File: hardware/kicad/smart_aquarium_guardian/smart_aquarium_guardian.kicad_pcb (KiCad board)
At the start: 2 copper layers, 110 x 90 mm, 30 parts, among them J1 Display_2.8_TFT_240xRGBx320, J2 Tiny_RTC_I2C_Module, J3 SensorsInput, J4 TdsMeter, J5 PowerSupply, M1 MountingHole_3.5mm, M2 MountingHole_3.5mm, M3 MountingHole_3.5mm, M4 MountingHole_3.5mm

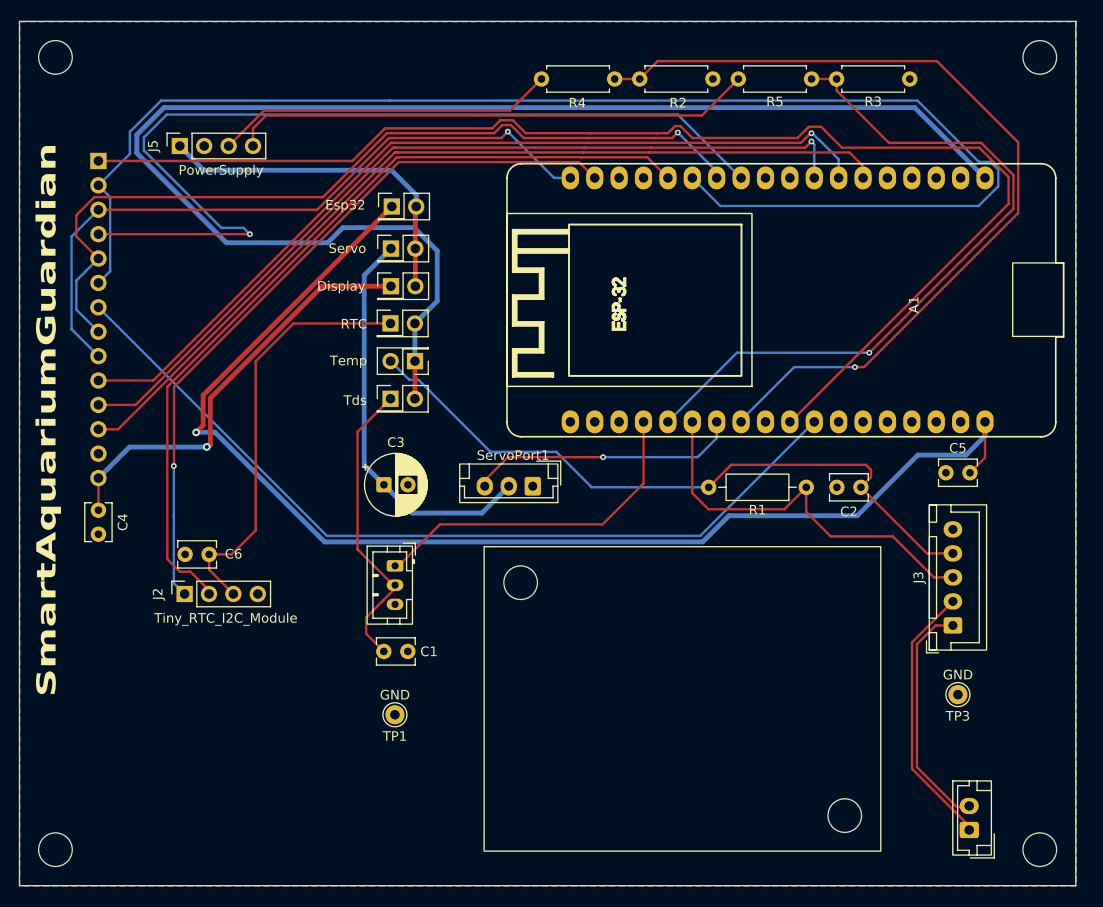
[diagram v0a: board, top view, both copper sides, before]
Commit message: Changes made after recommendations before printing it
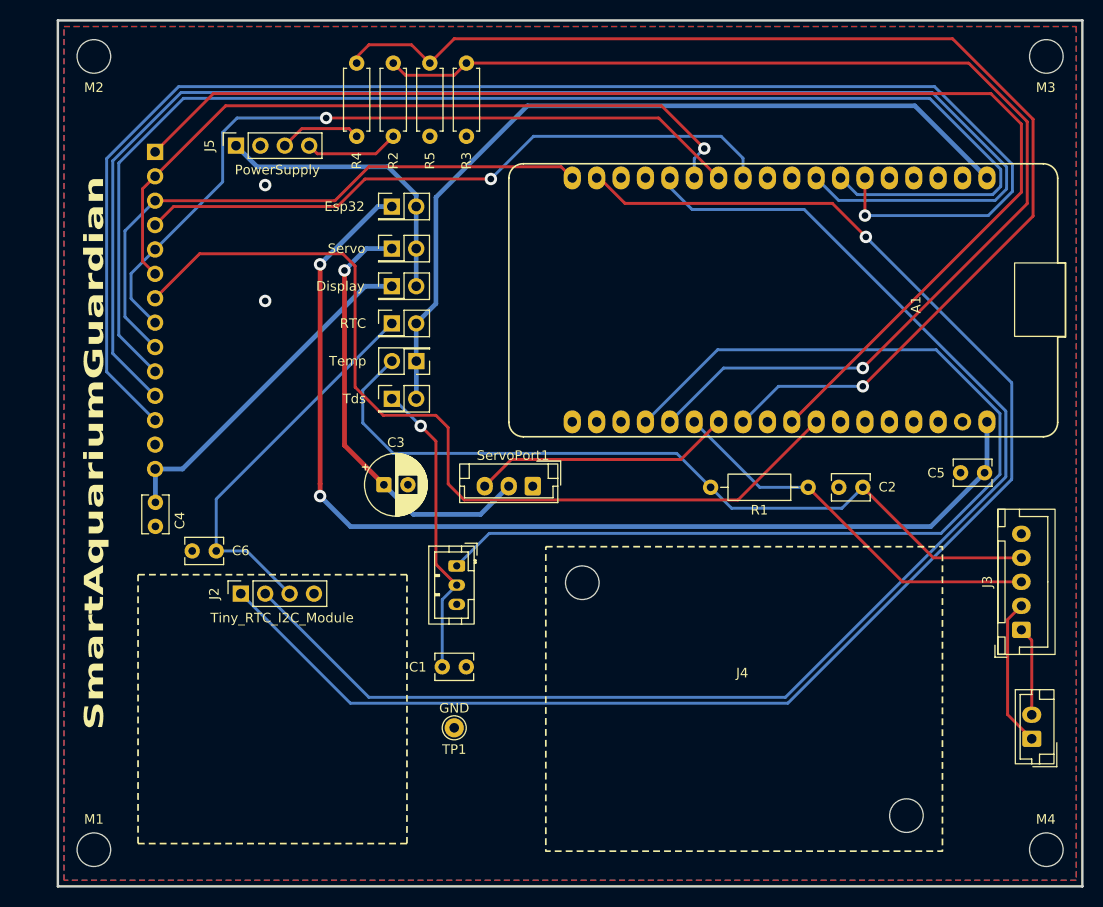
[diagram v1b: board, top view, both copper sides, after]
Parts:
- removed TP3: GND, Guardian:Pin_D1.0mm_L10.0mm
- moved R3 46.5 mm to (140.9, 60.5), turned to 90 degrees
- moved R5 43.6 mm to (133.3, 52.9), turned to -90 degrees
- moved R2 30.1 mm to (137.1, 60.5), turned to 90 degrees
- moved R4 26.9 mm to (129.5, 52.9), turned to -90 degrees
- moved J3 7.14 mm to (198.7, 111.9)
- moved J4 6.42 mm to (170.0, 117.7)
- moved TP1 6.32 mm to (139.6, 122.1)
- moved C1 6.29 mm to (138.4, 115.7)
- moved C4 5.99 mm to (108.5, 98.6)
- moved J1 5.98 mm to (108.5, 62.1)
- moved J2 5.85 mm to (117.4, 108.1)
- moved J5 5.85 mm to (116.9, 61.5)
- moved M2 4.00 mm to (102.1, 52.2)
- moved M1 4.00 mm to (102.1, 134.8)
- moved C5 1.53 mm to (192.3, 95.5)
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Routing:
- net Net-(A1-D22/SCL): track 76.2 -> 156.8 mm
- net Net-(A1-ADC1_CH6/D34): track 35.8 -> 109.6 mm
- net Net-(A1-D19): track 148.5 -> 76.8 mm, vias 0 -> 1
- net 3V3: track 147.6 -> 86.3 mm
- net Net-(A1-D15): track 93.4 -> 153.2 mm, vias 0 -> 1
- net Net-(A1-D4): track 89.5 -> 149.1 mm, vias 1 -> 0
- net Net-(A1-D21/SDA): track 86.9 -> 143.6 mm
- net Net-(A1-ADC1_CH7/D35): track 74.5 -> 124.8 mm
- net Net-(A1-D2): track 90.9 -> 140.5 mm, vias 1 -> 0
- net Net-(J5-VBAT): track 54.5 -> 9.86 mm
- net Net-(A1-DAC1/ADC2_CH8/D25): track 91.6 -> 126.1 mm
- net Net-(A1-D5): track 97.7 -> 68.0 mm
- net Net-(J5-VUSB): track 35.5 -> 8.55 mm
- net Net-(A1-VIN): track 130.8 -> 112.3 mm, vias 1 -> 2
- net Net-(J3-Pad1): track 24.4 -> 9.29 mm
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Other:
- board size 110 x 90 mm -> 106.7 x 90.2 mm

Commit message: Update smart_aquarium_guardian.kicad_pcb
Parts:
- removed C5: 100n, Guardian:C_Disc_D3.8mm_W2.6mm_P2.50mm
- added C7: 220u, Guardian:CP_Radial_D6.3mm_P2.50mm, F.Cu at (193.6, 96.7)
- moved J3 1.27 mm to (198.7, 113.2)
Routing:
- net Net-(J3-Pad2): track 15.5 -> 14.2 mm
- net Net-(J3-Pad1): track 9.29 -> 8.02 mm
- net Net-(A1-D21/SDA): track 143.6 -> 144.8 mm
- net Net-(A1-D22/SCL): track 156.8 -> 158.0 mm
- net Net-(A1-ADC1_CH6/D34): track 109.6 -> 110.8 mm
- net Net-(A1-ADC1_CH4/D32): track 41.0 -> 41.5 mm
- net Net-(JP4-B): track 83.9 -> 84.4 mm
